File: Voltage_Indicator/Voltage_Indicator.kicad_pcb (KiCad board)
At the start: 2 copper layers, 42.7 x 49.6 mm, 22 parts, among them IC1 TLV2371QDBVRQ1, J1 PET-02-XX-X-VT-LC, U2 IPBT-102-H1-XX-S-RA, U3 PAMC0381D10QDFXRQ1

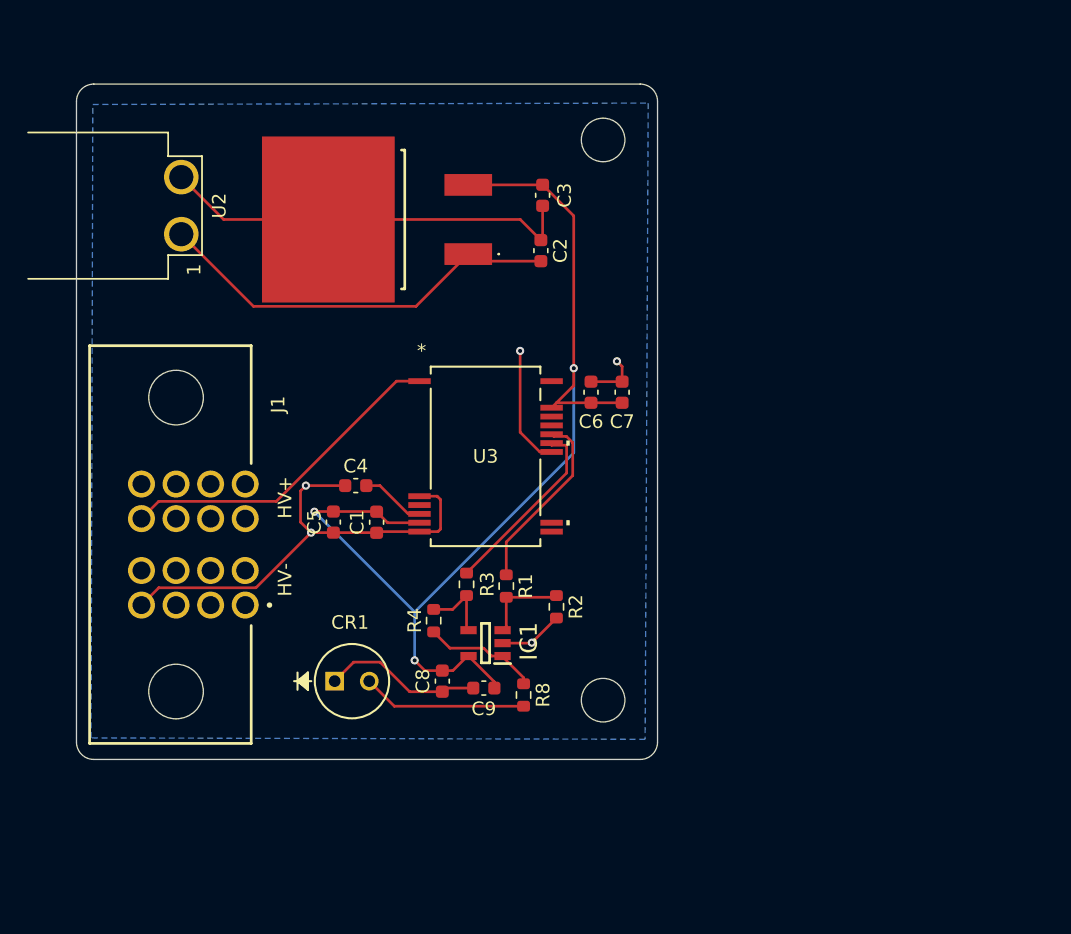
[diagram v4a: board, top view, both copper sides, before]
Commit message: Voltage Indicator with comparator :(
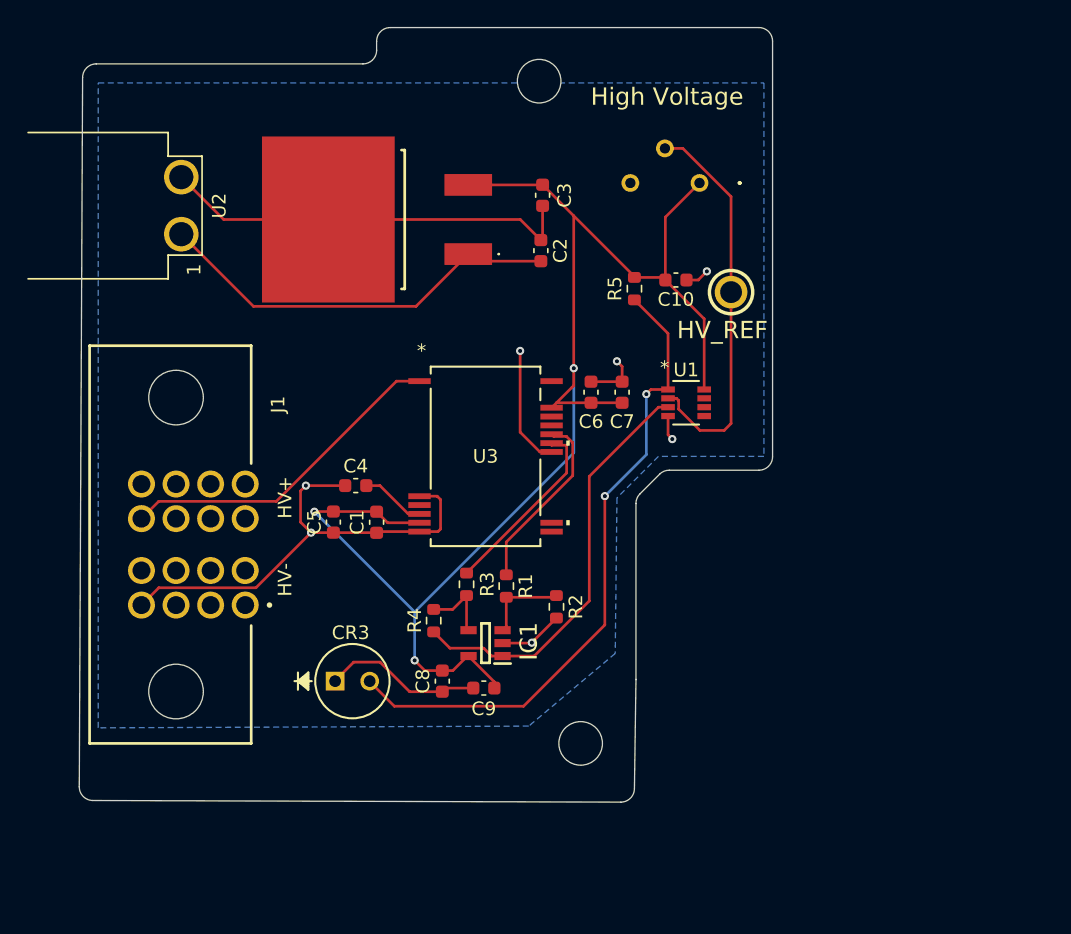
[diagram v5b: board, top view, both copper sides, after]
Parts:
- removed CR1: HLMP-EG08-WZ000, Footprints:LED_AVAGO_HLMP_XX08_AVA
- removed R8: 200, Resistor_SMD:R_0603_1608Metric
- removed the REF** at (173.5, 111.3)
- removed the REF** at (173.5, 70.1)
- added C10: 1uF, Capacitor_SMD:C_0603_1608Metric, F.Cu at (178.8, 80.4)
- added CR3: HLMP-EG08-WZ000, Footprints:LED_AVAGO_HLMP_XX08_AVA, F.Cu at (153.8, 109.9)
- added R5: 200, Resistor_SMD:R_0603_1608Metric, F.Cu at (175.8, 81.0)
- added RED_TP1: 5005, SDM_MiscFootprint:5005, F.Cu at (182.9, 81.3)
- added REF**: MountingHole_3.2mm_M3, MountingHole:MountingHole_3.2mm_M3, F.Cu at (168.8, 65.8)
- added REF**: MountingHole_3.2mm_M3, MountingHole:MountingHole_3.2mm_M3, F.Cu at (171.8, 114.4)
- added U1: LM393LVQDDFRQ1, Footprints:SOT-23-THIN8_DDF_TEX, F.Cu at (179.6, 89.4)
- added VR1: 10k, SDM_MiscFootprint:3386P1103TLF, F.Cu at (180.6, 73.3)
- C3: value 0.1uF -> 100nF
- R2, R4: value 10k -> 50k
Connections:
- net Net-(IC1-OUT) renamed /V_Out
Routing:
- net /HV_OUT: track 0.00 -> 48.1 mm, vias 0 -> 2
- net /HV_REF: track 0.00 -> 29.2 mm
- net +5V: track 80.9 -> 107.0 mm
- net /V_Out: track 8.47 -> 30.9 mm
- net Net-(CR1-Pad2): track 12.1 -> 0.00 mm
- net GND: track 60.2 -> 63.8 mm, vias 3 -> 5
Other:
- board size 42.7 x 49.6 mm -> 50.9 x 56.9 mm

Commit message: Fixed a net in BSPD and added isolated 5V line in voltage indicator
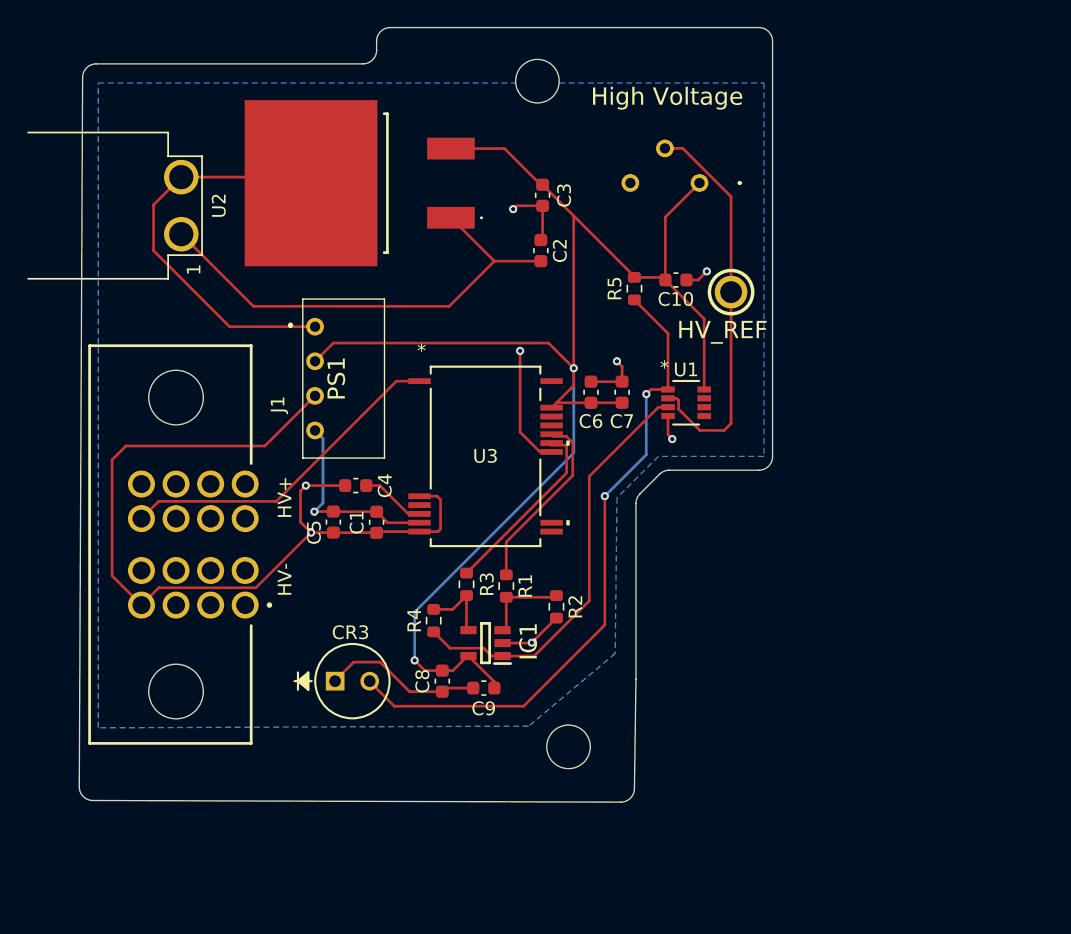
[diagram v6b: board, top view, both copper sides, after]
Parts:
- removed the REF** at (168.8, 65.8)
- removed the REF** at (171.8, 114.4)
- added PS1: TEA_1-0505, Footprints:TEA10505, F.Cu at (152.3, 83.8)
- added REF**: MountingHole_3.2mm_M3, MountingHole:MountingHole_3.2mm_M3, F.Cu at (168.7, 65.8)
- added REF**: MountingHole_3.2mm_M3, MountingHole:MountingHole_3.2mm_M3, F.Cu at (170.9, 114.7)
- moved CR2 2.95 mm to (155.4, 73.3)
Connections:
- C1 pad 2: +5V -> +5VDD
- C5 pad 2: +5V -> +5VDD
- U3 pad 5: +5V -> +5VDD
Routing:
- net /HV-: track 34.9 -> 63.4 mm
- net +5VDD: track 0.00 -> 14.6 mm, vias 0 -> 1
- net +5V: track 107.0 -> 111.2 mm, vias 3 -> 2
- net /12V Master: track 30.4 -> 34.5 mm
- net GND: track 63.8 -> 67.9 mm, vias 5 -> 6
